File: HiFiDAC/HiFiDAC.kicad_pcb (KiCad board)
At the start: 4 copper layers, 40 x 40 mm, 110 parts, among them J1 SE, J2 I2S, J3 LDIFF, J4 RDIFF, J5 CTRL, J6 5V, J7 +-15V, U1 PCM1794A, U2 TPS7A90, U3 OPA1612, U4 OPA1612, U5 OPA1612, U6 OPA1612, U7 OPA1612

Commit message: HiFiDAC redesign of clocking, digital IO, ferrite beads
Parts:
- removed the C11 at (32.5, 148.6)
- removed the J2 at (134.8, 86.3)
- removed the J5 at (65.4, 129.1)
- removed the R10 at (45.5, 162.4)
- removed the R12 at (36.5, 148.6)
- removed the R13 at (49.5, 152.3)
- removed the R14 at (36.5, 153.7)
- removed the R5 at (137.6, 90.0)
- removed the R6 at (136.0, 90.0)
- added C12: 0.1µF, Capacitor_SMD:C_0603_1608Metric, F.Cu at (92.3, 158.2)
- added C13: 10nF, Capacitor_SMD:C_0603_1608Metric, F.Cu at (92.3, 160.7)
- added C2: 10µF 50Vs, Capacitor_SMD:C_0805_2012Metric, F.Cu at (96.5, 163.0)
- added C20: 47µF 25V 750mΩ, Capacitor_SMD:CP_Elec_6.3x7.7, F.Cu at (83.1, 161.0)
- added C45: 0.1µF, Capacitor_SMD:C_0603_1608Metric, F.Cu at (79.8, 134.2)
- added C46: 0.1µF, Capacitor_SMD:C_0603_1608Metric, F.Cu at (79.8, 136.7)
- added C47: 1µF, Capacitor_SMD:C_0603_1608Metric, F.Cu at (79.8, 139.2)
- added C48: 1µF, Capacitor_SMD:C_0603_1608Metric, F.Cu at (79.8, 141.7)
- added C49: 0.1µF, Capacitor_SMD:C_0603_1608Metric, F.Cu at (79.8, 144.2)
- added C50: 100µF 10V 450mΩ, Capacitor_SMD:CP_Elec_6.3x7.7, F.Cu at (95.1, 137.0)
- added C51: 10µF 25V, Capacitor_SMD:C_0805_2012Metric, F.Cu at (92.1, 153.4)
- added C52: 0.1µF, Capacitor_SMD:C_0603_1608Metric, F.Cu at (79.8, 146.7)
- added FB1: MPZ1608B471ATA00, Inductor_SMD:L_0603_1608Metric, F.Cu at (79.8, 166.3)
- added FB2: MPZ1608B471ATA00, Inductor_SMD:L_0603_1608Metric, F.Cu at (83.9, 134.2)
- added FB3: MPZ1608B471ATA00, Inductor_SMD:L_0603_1608Metric, F.Cu at (83.9, 136.7)
- added J6: I2S, BW_Connectors:Amphenol_MINITEK_0.8_6P_V, F.Cu at (94.5, 143.3)
- added J7: CTRL, BW_Connectors:Amphenol_MINITEK_0.8_4P_V, F.Cu at (81.7, 150.2)
- added R45: 27Ω, Resistor_SMD:R_0603_1608Metric, F.Cu at (83.9, 139.2)
- added R46: 27Ω, Resistor_SMD:R_0603_1608Metric, F.Cu at (83.9, 141.7)
- added R47: 27Ω, Resistor_SMD:R_0603_1608Metric, F.Cu at (83.9, 144.2)
- added R48: 0Ω, Resistor_SMD:R_0603_1608Metric, F.Cu at (83.9, 146.7)
- added R49: 1kΩ, Resistor_SMD:R_0603_1608Metric, F.Cu at (87.9, 134.2)
- added R50: 33kΩ, Resistor_SMD:R_0603_1608Metric, F.Cu at (87.9, 136.7)
- added R51: 33kΩ, Resistor_SMD:R_0603_1608Metric, F.Cu at (87.9, 139.2)
- added R52: 1kΩ, Resistor_SMD:R_0603_1608Metric, F.Cu at (87.9, 141.7)
- added R53: 1kΩ, Resistor_SMD:R_0603_1608Metric, F.Cu at (87.9, 144.2)
- added U1: KC2520K24.5760, Oscillator:Oscillator_SMD_Kyocera_KC2520Z-4Pin_2.5x2.0mm, F.Cu at (96.3, 159.2)
- added U9: MAX14431C/F, Package_SO:QSOP-16_3.9x4.9mm_P0.635mm, F.Cu at (94.5, 148.7)
- C1: renamed from C4; value 47µF 20V -> 47µF 25V 750mΩ; footprint Capacitor_SMD:CP_Elec_5x5.8 -> Capacitor_SMD:CP_Elec_6.3x7.7
- R3: value 10Ω -> 0Ω
- R4: value 27Ω -> 0Ω
- moved R4 86.6 mm to (92.3, 165.7), turned to 0 degrees
- moved R3 83.6 mm to (92.3, 163.2), turned to 0 degrees
- moved C3 0.60 mm to (138.0, 101.2)
- moved C1 0.20 mm to (133.6, 101.2)
- renumbered C9 to C10, C10 to C11, C12 to C14, C13 to C15, C14 to C16, C15 to C17, C16 to C18, C17 to C19, C18 to C21, C19 to C22, C20 to C23, C21 to C24, C22 to C25, C23 to C26, C24 to C27, C25 to C28, C26 to C29, C5 to C3, C27 to C30, C28 to C31, C29 to C32, C30 to C33, C31 to C34, C32 to C35, C33 to C36, C34 to C37, C35 to C38, C36 to C39, C1 to C4, C37 to C40, C38 to C41, C39 to C42, C40 to C43, C41 to C44, C2 to C5, C3 to C6, C6 to C7, C7 to C8, C8 to C9, J3 to J2, J4 to J3, J6 to J4, J7 to J5, R16 to R10, R17 to R11, R18 to R12, R19 to R13, R20 to R14, R21 to R15, R22 to R16, R23 to R17, R24 to R18, R25 to R19, R26 to R20, R27 to R21, R28 to R22, R29 to R23, R30 to R24, R31 to R25, R32 to R26, R33 to R27, R34 to R28, R35 to R29, R36 to R30, R37 to R31, R38 to R32, R39 to R33, R40 to R34, R41 to R35, R42 to R36, R43 to R37, R44 to R38, R45 to R39, R46 to R40, R47 to R41, R48 to R42, R49 to R43, R50 to R44, R7 to R5, R8 to R6, R9 to R7, R11 to R8, R15 to R9, U1 to U2, U2 to U3, U3 to U4, U4 to U5, U5 to U6, U6 to U7, U7 to U8
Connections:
- C21 pad 1: +5V -> Net-(U3-EN)
- R3 pad 1: Net-(J2-Pin_2) (its old number) -> Net-(U1-CLK)
- R4 pad 1: Net-(J2-Pin_3) -> /Digital Interface/SCK
- R4 pad 2: Net-(U1-BCK) -> Net-(U1-CLK)
- U2 pad 10: Net-(U1-MUTE) -> /Digital Interface/MUTE
- U2 pad 14: Net-(U1-~{RST}) -> /Digital Interface/~{RST}
- U2 pad 4: Net-(U1-LRCK) -> /Digital Interface/LRCK
- U2 pad 5: Net-(U1-DATA) -> /Digital Interface/DATA
- U2 pad 6: Net-(U1-BCK) -> /Digital Interface/BCK
- U3 pad 10: +5V -> Net-(U3-EN)
- U3 pad 6: +5V -> Net-(U3-EN)
- U3 pad 7: +5V -> Net-(U3-EN)
- U3 pad 9: +5V -> Net-(U3-EN)

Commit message: HiFiDAC initial layout complete
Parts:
- C1: value 47µF 25V 750mΩ -> 100µF 10V 450mΩ
- C20: value 47µF 25V 750mΩ -> 100µF 10V 450mΩ; moved to B.Cu
- C47, C48, C49, C50, C51, C52, FB1, FB3, JP1, JP2, JP3, JP4, JP5, R10, R11, R12, R13, R14, R49, R50, R52, R53: moved to B.Cu
- moved R10 124.9 mm to (145.6, 97.9), turned to 90 degrees
- moved R11 124.5 mm to (145.3, 100.7)
- moved R14 114.5 mm to (145.3, 107.7)
- moved R12 114.2 mm to (145.3, 103.3)
- moved R13 114.1 mm to (145.3, 105.9)
- moved J7 94.0 mm to (147.2, 82.8)
- moved JP5 94.0 mm to (142.0, 108.5)
- moved JP4 93.4 mm to (142.0, 105.9)
- moved JP3 92.9 mm to (142.0, 103.3)
- moved JP1 92.6 mm to (142.9, 98.1)
- moved JP2 92.3 mm to (142.0, 100.7)
- moved C47 88.7 mm to (150.1, 85.0), turned to 180 degrees
- moved C48 87.8 mm to (146.9, 85.0), turned to 180 degrees
- moved C49 87.1 mm to (144.4, 85.8), turned to -90 degrees
- moved R4 84.3 mm to (137.2, 94.3), turned to -90 degrees
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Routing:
- added copper zone on B.Cu, net /Digital Interface/GND_EXT
- added copper zone on F.Cu, net /Digital Interface/GND_EXT
- added copper zone on In1.Cu, net /Digital Interface/GND_EXT
- added copper zone on In2.Cu, net /Digital Interface/GND_EXT
- added copper zone on B.Cu, net GND
- added copper zone on F.Cu, net GND
- added copper zone on In1.Cu, net GND
- added copper zone on In2.Cu, net GND

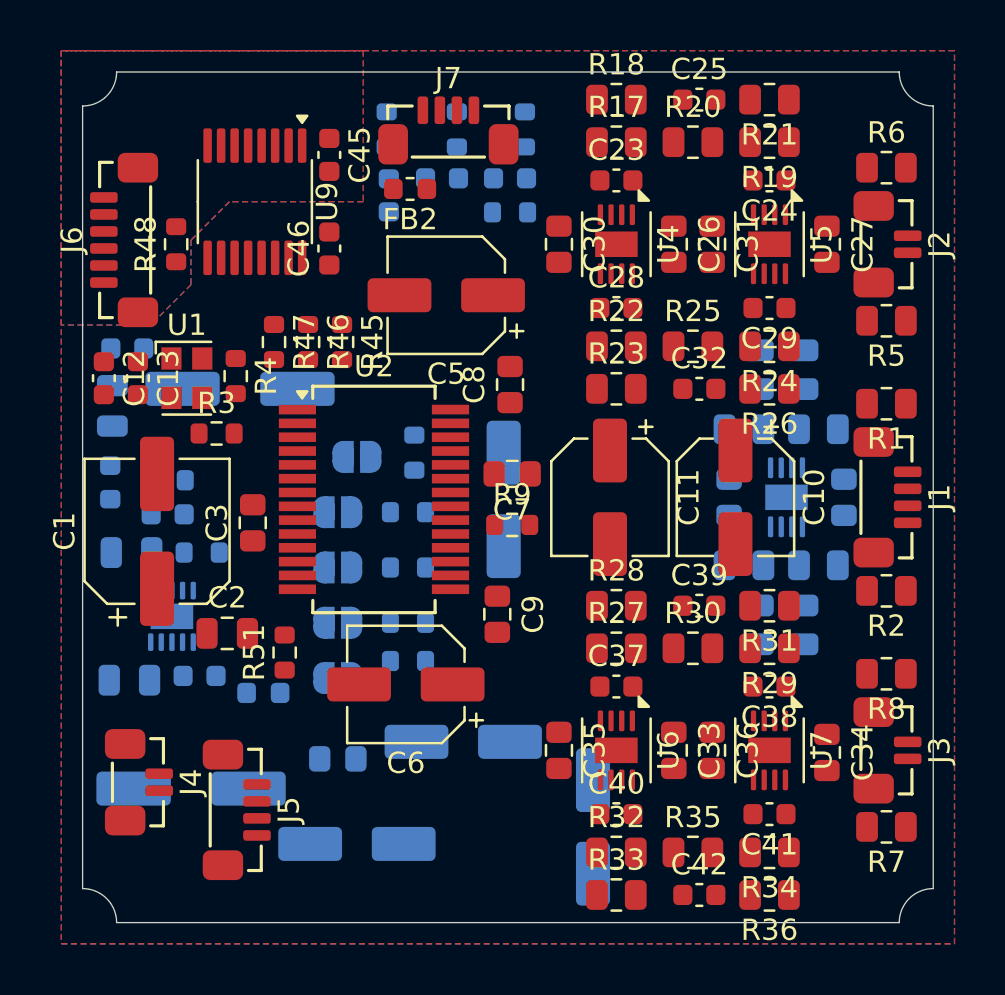
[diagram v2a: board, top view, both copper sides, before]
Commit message: HiFiDAC routing initially complete
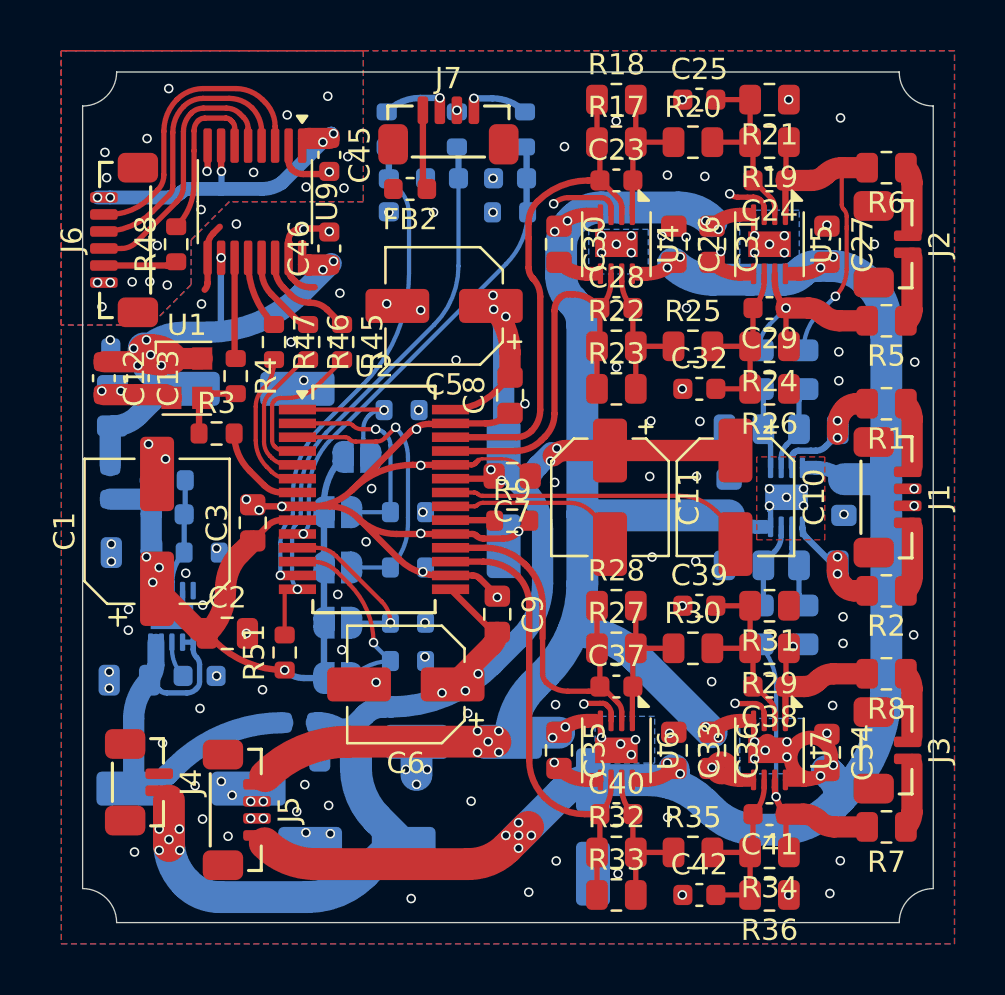
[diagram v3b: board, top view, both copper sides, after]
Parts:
- moved FB1 2.20 mm to (140.2, 110.6)
- moved R10 2.09 mm to (145.0, 95.9), turned to 0 degrees
- moved C5 0.51 mm to (147.0, 91.0)
- moved C8 0.50 mm to (150.1, 95.2)
- moved R9 0.20 mm to (150.2, 101.1)
- moved C7 0.10 mm to (150.2, 99.0)
- turned R6 to 180 degrees
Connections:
- R1 pad 1: Net-(J1-Pin_1) -> Net-(J1-Pin_4)
- R2 pad 1: Net-(J1-Pin_4) -> Net-(J1-Pin_1)
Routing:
- net -15V: track 0.00 -> 82.8 mm, vias 0 -> 37
- net +15V: track 0.00 -> 80.7 mm, vias 0 -> 13
- net +5V: track 0.00 -> 76.8 mm, vias 0 -> 15
- net GND: track 0.00 -> 76.8 mm, vias 0 -> 124
- net +3.3V: track 0.00 -> 35.0 mm, vias 0 -> 4
- net +3.3VD: track 0.00 -> 29.7 mm, vias 0 -> 8
- net /Digital Interface/~{RST}: track 0.00 -> 26.3 mm, vias 0 -> 1
- net /I-V Stage/IL-: track 0.00 -> 24.1 mm
- net /ZERO: track 0.00 -> 23.1 mm, vias 0 -> 1
- net /Digital Interface/MUTE: track 0.00 -> 22.6 mm, vias 0 -> 1
- net /I-V Stage/IR+: track 0.00 -> 22.4 mm
- net Net-(U3-EN): track 0.00 -> 20.8 mm
- net /I-V Stage/IL+: track 0.00 -> 19.0 mm
- net /I-V Stage/IR-: track 0.00 -> 18.1 mm
- net /Differential Amp/VL-: track 0.00 -> 16.7 mm, vias 0 -> 1
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- added copper zone on B.Cu, net -15V
- added copper zone on F.Cu, net -15V

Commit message: HiFiDAC PCB reference placement, text, and cleanup
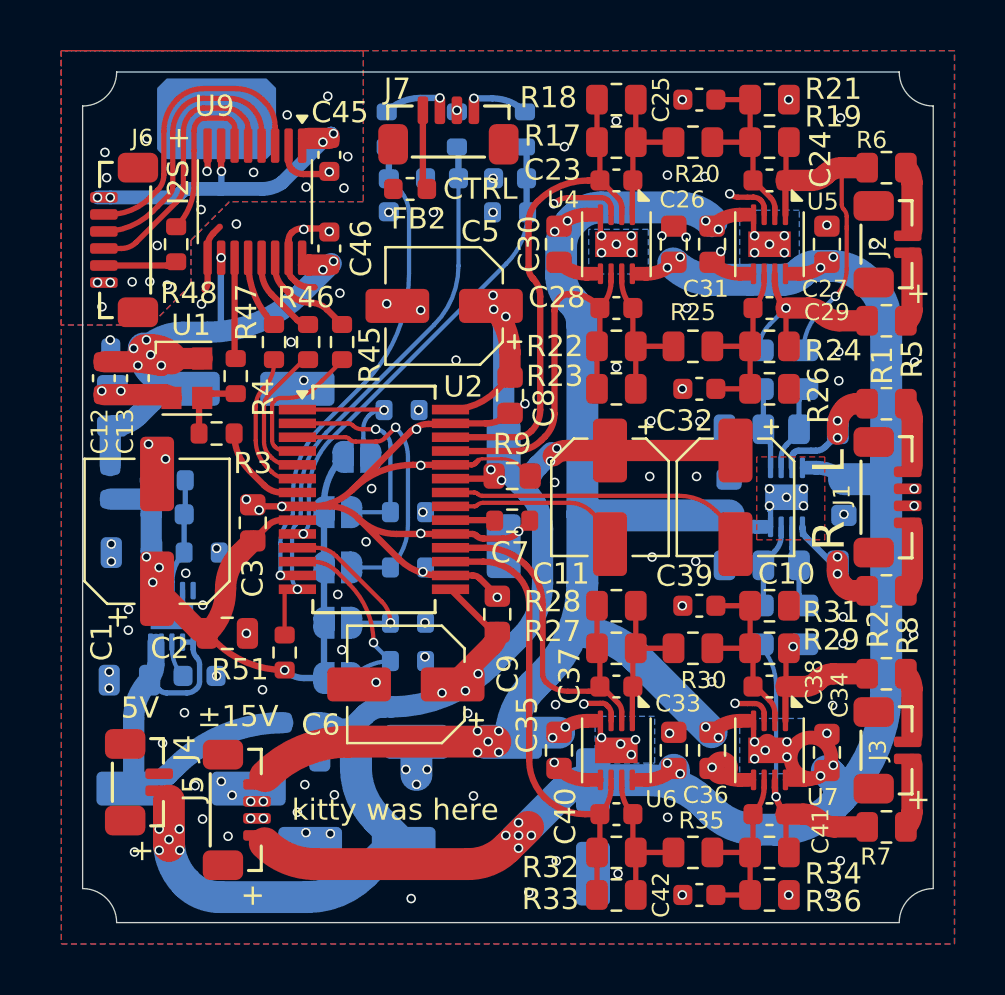
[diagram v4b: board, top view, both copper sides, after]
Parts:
- added REF**: BW_Logo_5x3.2mm, BW_Logo:BW_Logo_5x3.2mm, B.Cu at (136.3, 82.2)
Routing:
- net /Digital Interface/GND_EXT: vias 20 -> 19
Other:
- board text added: "+"
- board text added: "5V"
- board text added: "CHSL"
- board text added: "CTRL"
- board text added: "DEM"
- board text added: "FMT 0 1"
- board text added: "I2S +"
- board text added: "L"
- board text added: "MONO"
- board text added: "Modular Audio HiFi DAC"
- board text added: "R"
- board text added: "kitty was here"
- board text added: "±15V"

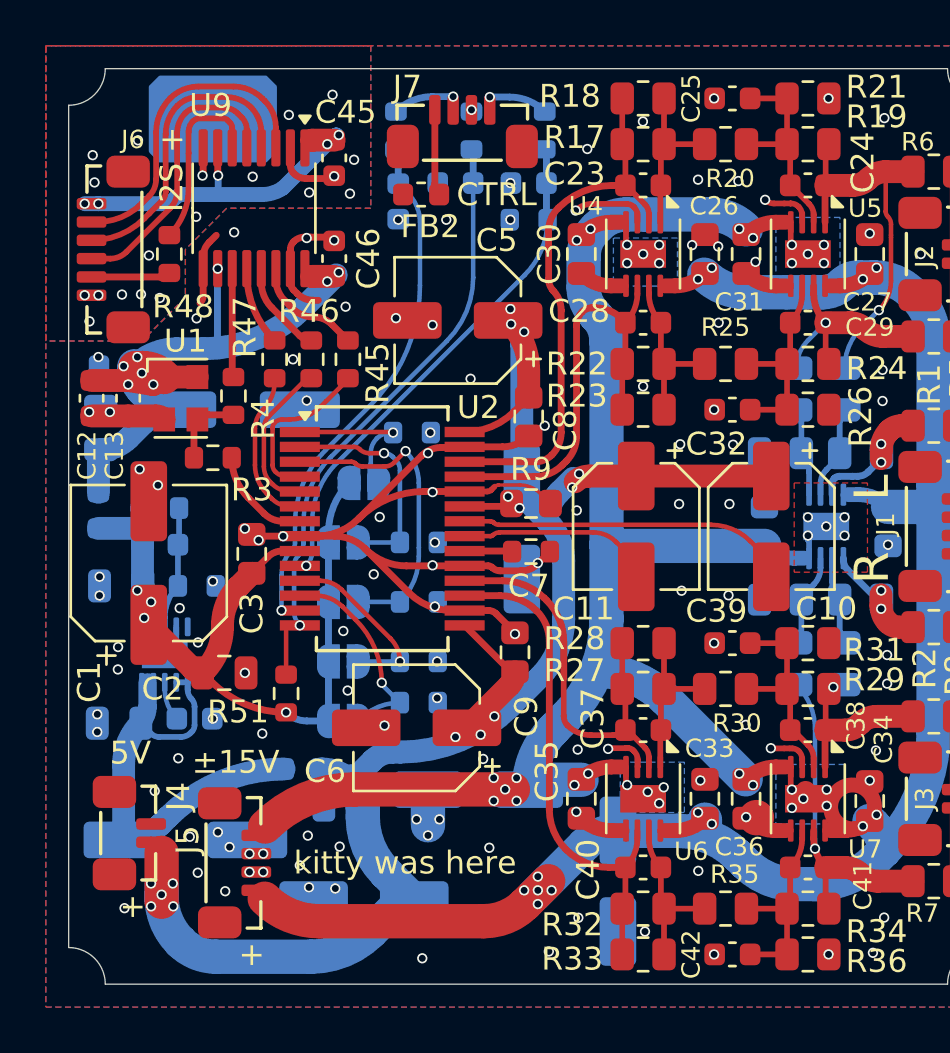
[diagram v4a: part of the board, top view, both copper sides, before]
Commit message: HiFiDAC routing done, CleanLVSupply fuses added
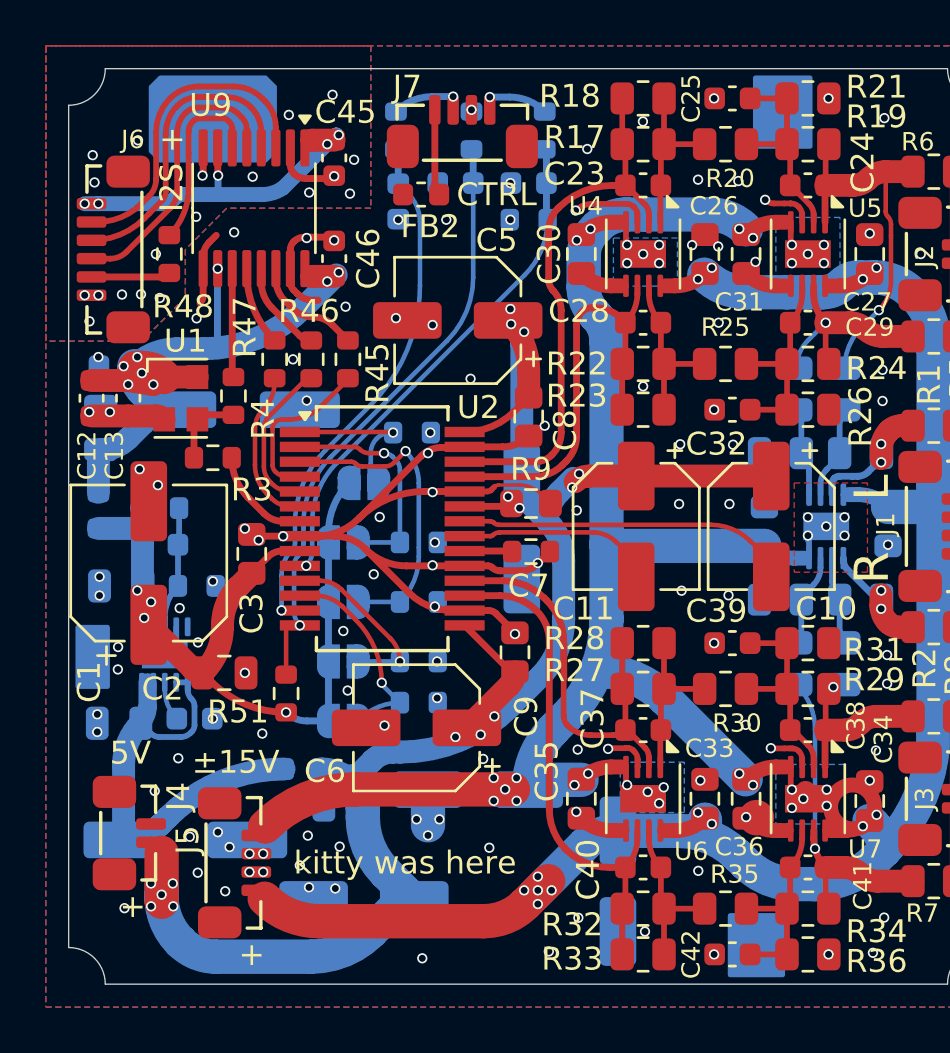
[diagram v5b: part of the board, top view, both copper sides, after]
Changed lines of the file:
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@@
 		(tags "capacitor")
 		(property "Reference" "C21"
-			(at 1 2.3 -90)
+			(at 1.3 -2.3 -90)
 			(layer "B.SilkS")
 			(effects
@@
 			(net 2 "GND")
 			(pintype "passive")
+			(zone_connect 2)
 		)
 		(model "${KICAD8_3DMODEL_DIR}/Capacitor_SMD.3dshapes/C_0805_2012Metric.wrl"
@@
 		(tags "capacitor")
 		(property "Reference" "C19"
-			(at 1 -1.7 360)
+			(at 0.8 1.4 360)
 			(layer "B.SilkS")
 			(effects
@@
 			(net 2 "GND")
 			(pintype "passive")
+			(zone_connect 2)
 		)
 		(model "${KICAD8_3DMODEL_DIR}/Capacitor_SMD.3dshapes/C_0805_2012Metric.wrl"
@@
 		)
 	)
+	(gr_rect
+		(start 158.9 117)
+		(end 161.2 119.6)
+		(stroke
+			(width 0.2)
+			(type default)
+		)
+		(fill solid)
+		(layer "B.Cu")
+	)
+	(gr_rect
+		(start 130.4 104.4)
+		(end 131.7 107)
+		(stroke
+			(width 0.2)
+			(type default)
+		)
+		(fill solid)
+		(layer "B.Cu")
+	)
+	(gr_rect
+		(start 160 80.4)
+		(end 162.4 83.4)
+		(stroke
+			(width 0.2)
+			(type default)
+		)
+		(fill solid)
+		(layer "B.Cu")
+	)
+	(gr_rect
+		(start 158.9 117)
+		(end 161.2 119.6)
+		(stroke
+			(width 0.1)
+			(type default)
+		)
+		(fill solid)
+		(layer "B.Mask")
+	)
+	(gr_rect
+		(start 160 80.4)
+		(end 162.4 83.4)
+		(stroke
+			(width 0.1)
+			(type default)
+		)
+		(fill solid)
+		(layer "B.Mask")
+	)
+	(gr_rect
+		(start 153 80.4)
+		(end 155.4 83.4)
+		(stroke
+			(width 0.1)
+			(type default)
+		)
+		(fill solid)
+		(layer "B.Mask")
+	)
+	(gr_rect
+		(start 130.4 104.4)
+		(end 131.7 107)
+		(stroke
+			(width 0.1)
+			(type default)
+		)
+		(fill solid)
+		(layer "B.Mask")
+	)
+	(gr_rect
+		(start 147 116.6)
+		(end 149.4 119.6)
+		(stroke
+			(width 0.1)
+			(type default)
+		)
+		(fill solid)
+		(layer "B.Mask")
+	)
 	(gr_line
 		(start 130 81.6)
@@
 	)
 	(via
-		(at 133.51 88.16)
+		(at 133.81 88.1)
 		(size 0.45)
 		(drill 0.3)
